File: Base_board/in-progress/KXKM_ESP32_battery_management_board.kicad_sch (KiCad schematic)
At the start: 44 parts, among them J1 Conn_01x06, J11 TEST_1P, J2 TEST_1P, J3 Conn_02x10_Odd_Even, J4 Conn_01x04, J6 Conn_01x03, J7 Conn_01x03, J8 Conn_01x03, Q1 BC847W, Q2 BC847W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

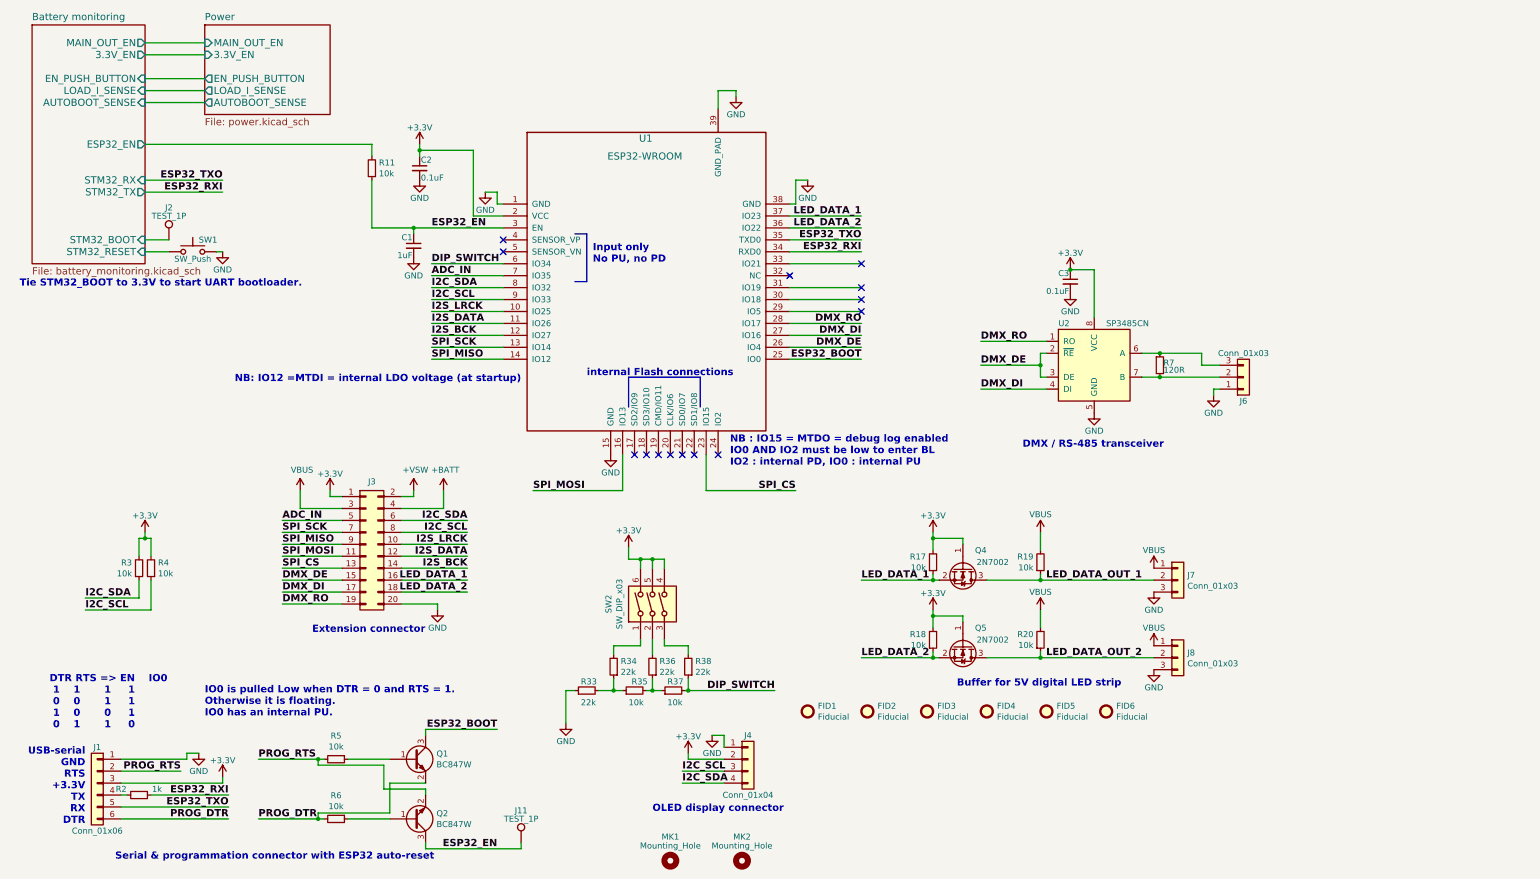
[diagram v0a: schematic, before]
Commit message: update v3.2
-  connecteur XT60 coudé (et disponible chez JLCPCB)
- modification de l’autoboot pour un redémarrage en cas de perte brêve d’alimentation,
- ajout de l’empreinte pour rajouter une lecteur microSD
- mise à jour des piste de sortie batterie conforme pour 10A
- suppression des pin I2C (déjà dispo sur le GPIO)
- connecteur JST B3B-EH pour un câblage et éviter les soudure qui casse sur les sortie pour LED
- ESP32 en version 16M
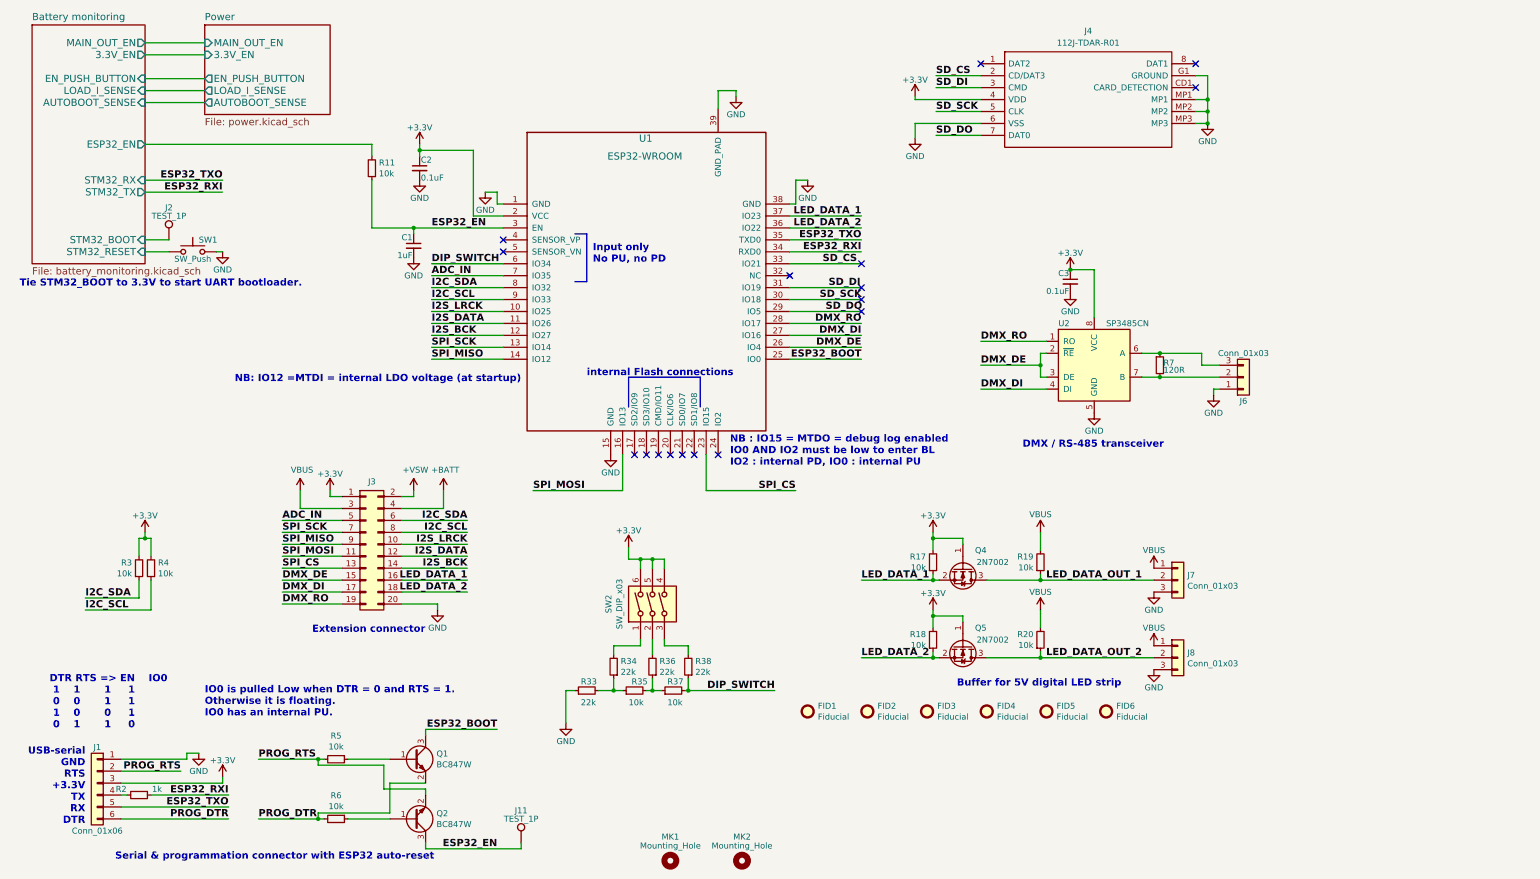
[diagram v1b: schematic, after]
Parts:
- removed J4: Conn_01x04, Connector_PinSocket_2.54mm:PinSocket_1x04_P2.54mm_Vertical, symbol Connector_Generic:Conn_01x04
- added J4: 112J-TDAR-R01, 112JTDARR01, symbol 112J-TDAR-R01:112J-TDAR-R01
- C1: LCSC (none) -> C15849
- C2, C3: LCSC (none) -> C14663
- J7, J8: footprint tom_kicad_lib:SolderWirePad_1x03_P3.81mm_Drill1.2mm -> Connector_JST:JST_EH_B3B-EH-A_1x03_P2.50mm_Vertical
- Q1, Q2: LCSC (none) -> C130418
- Q4, Q5: LCSC (none) -> C8545
- R11, R17, R18, R19, R20, R3, R35, R37, R4, R5, R6: LCSC (none) -> C25804
- R2: LCSC (none) -> C21190
- R33, R34, R36, R38: LCSC (none) -> C31850
- R7: LCSC (none) -> C114681
- SW1: LCSC (none) -> C128941
- SW2: LCSC (none) -> C319070
- U1: LCSC (none) -> C529580
- U2: LCSC (none) -> C668205
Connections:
- net +3V3: now also J4.4 (VDD)
- net GND: now also J4.6 (VSS), J4.G1 (GROUND), J4.MP1, J4.MP2, J4.MP3
- net SD_DO: now reaches U1.29 (IO5)
- net SD_DO: now also J4.7 (DAT0)
- net SD_SCK: now reaches U1.30 (IO18)
- net SD_SCK: now also J4.5 (CLK)
- net SD_DI: now reaches U1.31 (IO19)
- net SD_DI: now also J4.3 (CMD)
- net SD_CS: now reaches U1.33 (IO21)
- net SD_CS: now also J4.2 (CD/DAT3)
- no-connect marks 14 -> 17
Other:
- note removed: "OLED display connector"

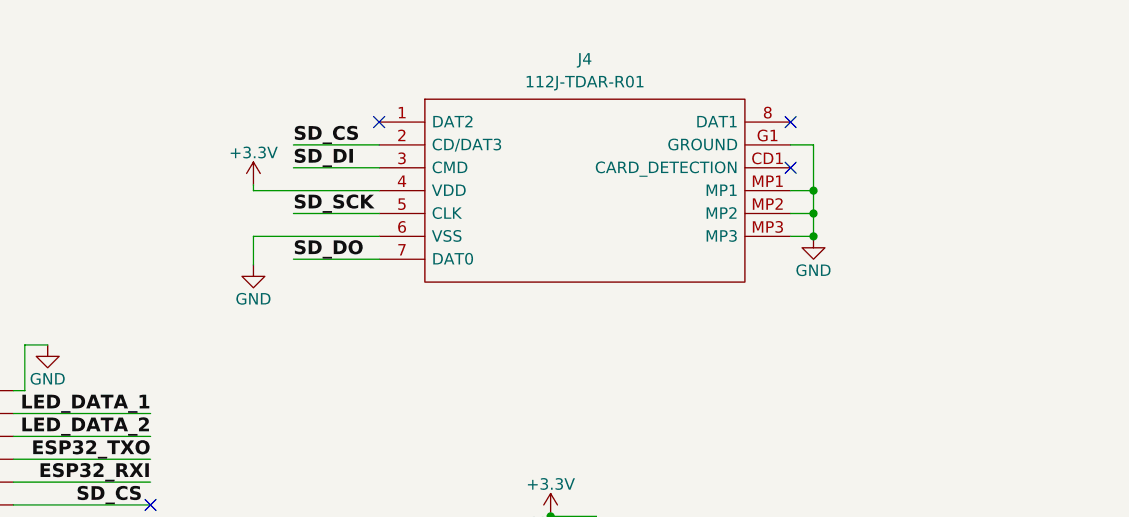
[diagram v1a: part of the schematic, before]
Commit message: update casing
better file naming
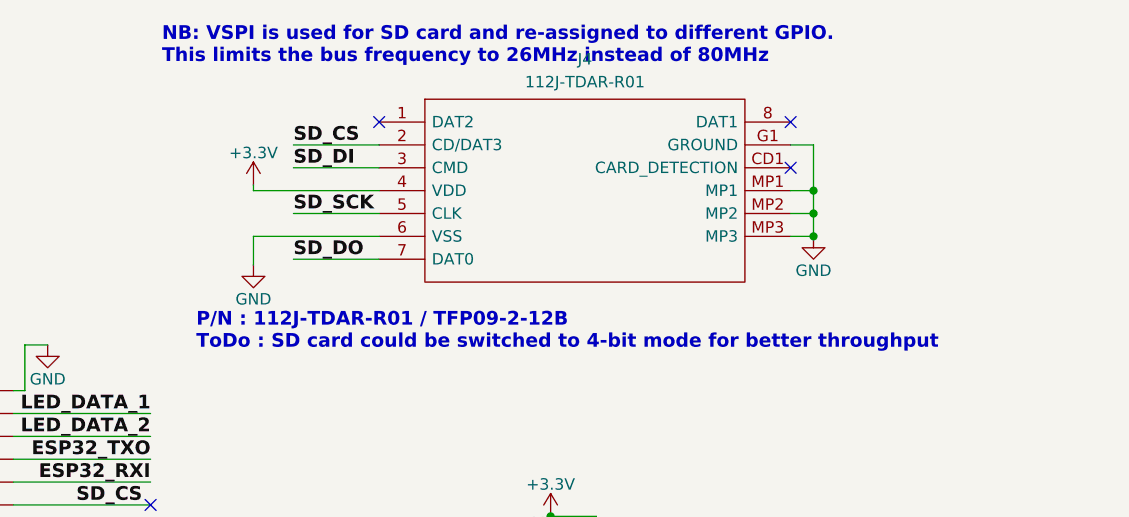
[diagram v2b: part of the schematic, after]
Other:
- note added: "NB: VSPI is used for SD card and re-assigned to different GPIO. This limits the bus frequency to 26MHz instead of 80MHz"
- note added: "P/N : 112J-TDAR-R01 / TFP09-2-12B ToDo : SD card could be switched to 4-bit mode for better throughput"
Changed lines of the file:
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@@
     (stroke (width 0) (type default))
+  )
+  (text "NB: VSPI is used for SD card and re-assigned to different GPIO.\nThis limits the bus frequency to 26MHz instead of 80MHz"
+    (at 193.04 18.415 0)
+    (effects (font (size 1.524 1.524) (thickness 0.3048) bold) (justify left bottom))
   )
   (text "DMX / RS-485 transceiver" (at 226.06 106.68 0)
@@
     (effects (font (size 1.524 1.524) (thickness 0.3048) bold) (justify left bottom))
   )
+  (text "P/N : 112J-TDAR-R01 / TFP09-2-12B \nToDo : SD card could be switched to 4-bit mode for better throughput"
+    (at 196.85 50.165 0)
+    (effects (font (size 1.524 1.524) (thickness 0.3048) bold) (justify left bottom))
+  )

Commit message: update to v3.2 and casing 3D View
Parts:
- J7, J8: LCSC (none) -> C398546
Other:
- note added: "ref de connecteur précablé : CABLE-EH03 TODO : améliorer le type de connecteur avec un cablage trouvable facilement/pas chère"
- company: KXKM -> for : KXKM
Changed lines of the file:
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@@
     (date "2023-06-14")
     (rev "3.2")
-    (company "KXKM")
-    (comment 1 "Tom Magnier / initial release")
-    (comment 2 "Viven Henry / SD, Switch, Autoboot")
-    (comment 3 "Clément SAILLANT / update Autoboot, readd SD")
+    (company "for : KXKM")
+    (comment 1 "update PCB, add optional SD, ....")
+    (comment 2 "Clément SAILLANT (v3.2) : improve Autoboot")
+    (comment 3 "Viven Henry (v3) : remove SD, add Switch, add Autoboot")
+    (comment 4 "Tom Magnier :  initial release (v1 & v2)")
   )
   (junction (at 154.94 158.115) (diameter 0) (color 0 0 0 0)
@@
     (at 119.38 92.71 0)
     (effects (font (size 1.524 1.524) (thickness 0.3048) bold) (justify right bottom))
+  )
+  (text "ref de connecteur précablé :\nCABLE-EH03\n\nTODO :\n\naméliorer le type de connecteur\navec un cablage trouvable facilement/pas chère"
+    (at 264.795 147.32 0)
+    (effects (font (size 1.524 1.524) (thickness 0.3048) bold) (justify left bottom))
   )
   (text "internal Flash connections" (at 133.35 91.44 0)
@@
       (effects (font (size 1.27 1.27)) hide)
     )
-    (property "LCSC" "" (at 259.08 134.62 0)
+    (property "LCSC" "C398546" (at 259.08 134.62 0)
       (effects (font (size 1.27 1.27)) hide)
     )
@@
       (effects (font (size 1.27 1.27)) hide)
     )
-    (property "LCSC" "" (at 259.08 151.13 0)
-      (effects (font (size 1.27 1.27)) hide)
-    )
+    (property "LCSC" "C398546" (at 259.08 151.13 0)
+      (effects (font (size 1.27 1.27)) hide)
+    )
